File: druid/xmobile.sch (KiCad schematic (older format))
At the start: 12 parts, among them P3 CONN_8

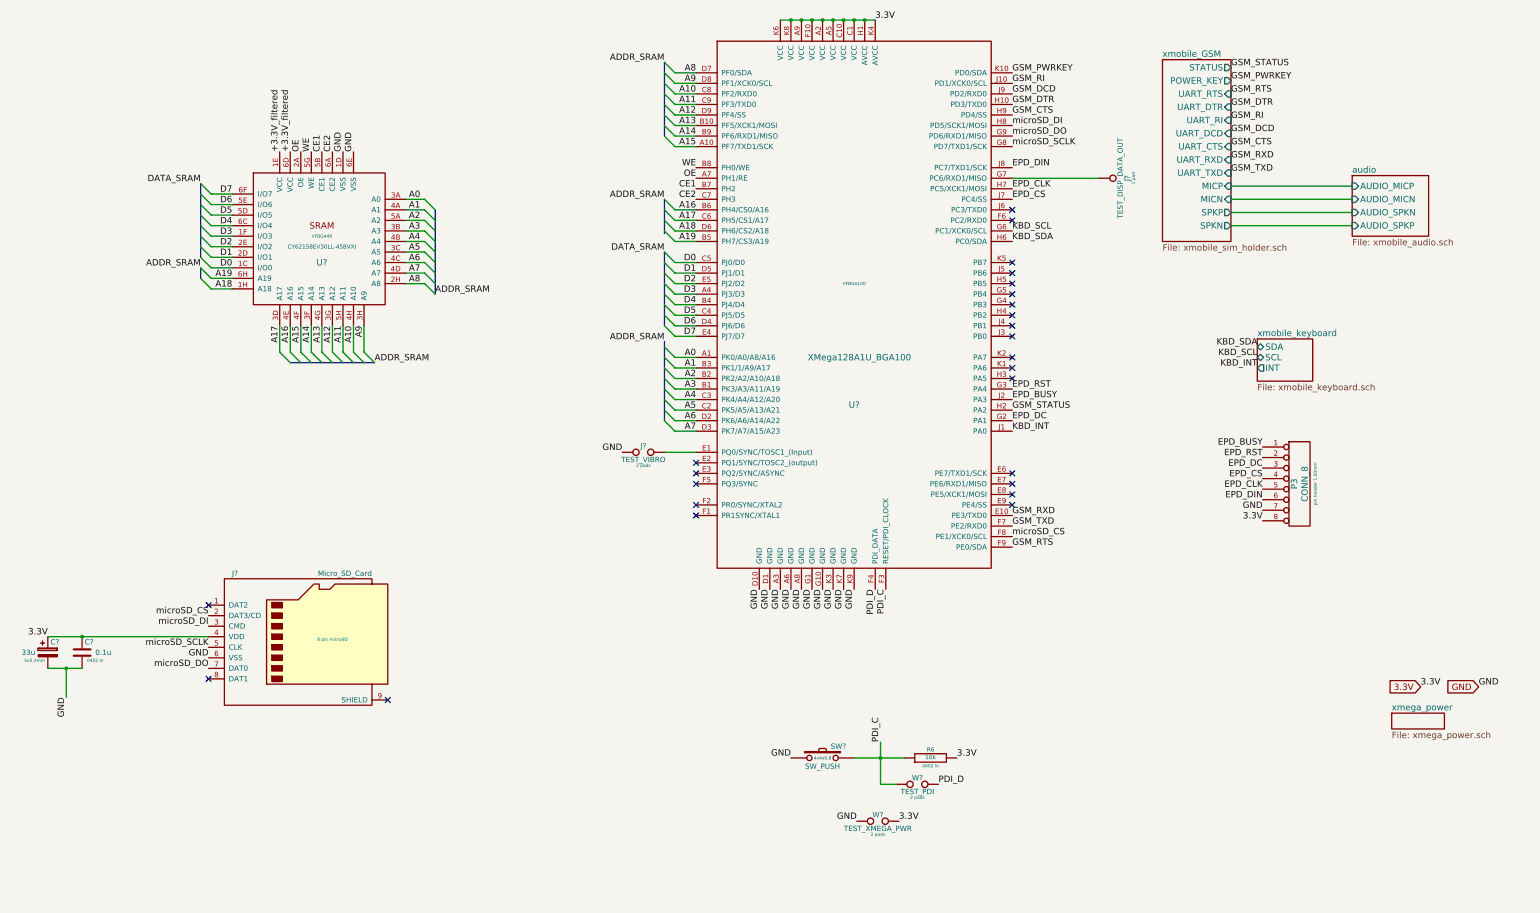
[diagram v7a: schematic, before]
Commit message: remove electric  warnings and errors. annotate elements. fix microUSB-B symbol.
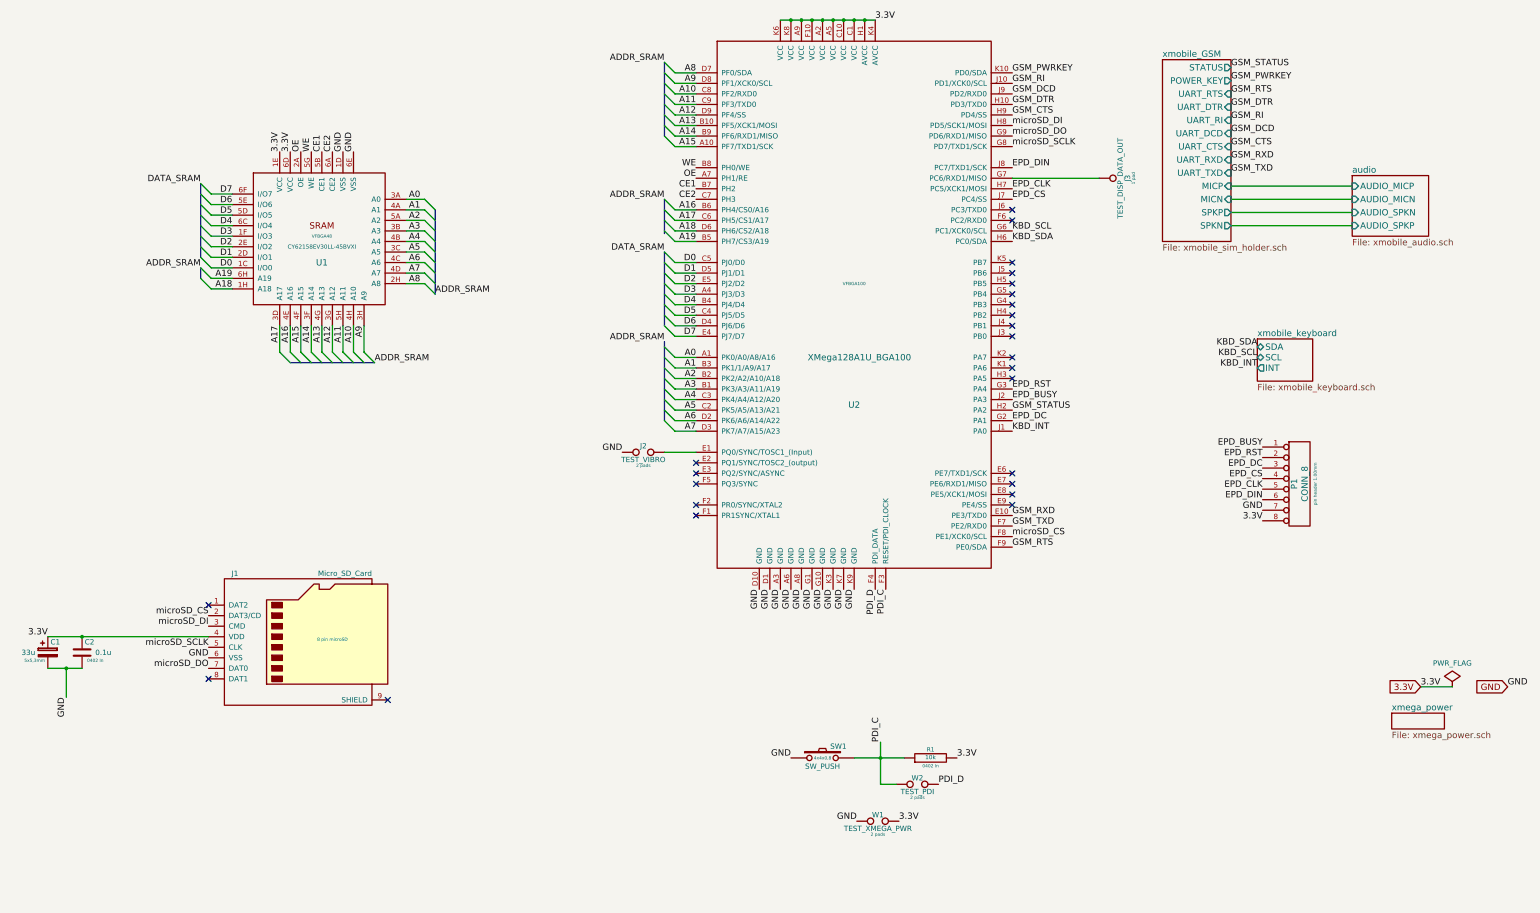
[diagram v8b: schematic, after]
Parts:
- gave numbers to parts that had none: 10
- renumbered P3 to P1, R6 to R1
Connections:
- net +3.3V_filtered is gone; now on net 3.3V: U1.1E (VCC), U1.6D (VCC)
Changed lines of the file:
@@
 $EndDescr
 $Comp
-L xmobile-rescue:R-RESCUE-xmobile R6
+L xmobile-rescue:R-RESCUE-xmobile R1
 U 1 1 5967CB22
 P 10025 10100
-F 0 "R6" V 10105 10100 40  0000 C CNN
+F 0 "R1" V 10105 10100 40  0000 C CNN
 F 1 "10k" V 10032 10101 40  0000 C CNN
 F 2 "Resistors_SMD:R_0402" V 9955 10100 30  0001 C CNN
@@
 3.3V
 $Comp
-L xmobile-rescue:CONN_8 P3
+L xmobile-rescue:CONN_8 P1
 U 1 1 5974D7B3
 P 13525 7500
-F 0 "P3" V 13475 7500 60  0000 C CNN
+F 0 "P1" V 13475 7500 60  0000 C CNN
 F 1 "CONN_8" V 13575 7500 60  0000 C CNN
 F 2 "Connector_Pin_Header_1.00mm:PinHeader_1x08_P1.00mm_Vertical" V 13700 7450 60  0001 C CNN
@@
 PDI_C
 $Comp
-L xmobile-rescue:CY62158EV30LL-45BVXI U?
+L xmobile-rescue:CY62158EV30LL-45BVXI U1
 U 1 1 5C118522
 P 4250 5200
-F 0 "U?" H 4250 5000 60  0000 C CNN
+F 0 "U1" H 4250 5000 60  0000 C CNN
 F 1 "CY62158EV30LL-45BVXI" H 4250 5150 39  0000 C CNN
 F 2 "druid:48-ball_VFBGA_6x8x1mm_BV48BZ48" H 4475 3925 60  0001 C CNN
@@
 $EndComp
 $Comp
-L xmobile-rescue:XMega128A1U_BGA100 U?
+L xmobile-rescue:XMega128A1U_BGA100 U2
 U 1 1 5C19D697
 P 9300 5600
-F 0 "U?" H 9300 4450 60  0000 C CNN
+F 0 "U2" H 9300 4450 60  0000 C CNN
 F 1 "XMega128A1U_BGA100" H 9350 4900 60  0000 C CNN
 F 2 "druid:BGA100_9x9x1.2_pitch-0.80mm" H 9400 5150 60  0001 C CNN
@@
 PDI_D
 Text Label 3850 4350 1    60   ~ 0
-+3.3V_filtered
+3.3V
 Text Label 3950 4350 1    60   ~ 0
-+3.3V_filtered
+3.3V
 Text Label 4550 4350 1    60   ~ 0
 GND
@@
 KBD_INT
 $Comp
-L xmobile-rescue:TEST_1P J?
+L xmobile-rescue:TEST_1P J3
 U 1 1 5C4B9CCC
 P 11625 4600
-F 0 "J?" H 11625 4870 50  0000 C CNN
+F 0 "J3" H 11625 4870 50  0000 C CNN
 F 1 "TEST_DISP_DATA_OUT" H 11625 4800 50  0000 C CNN
 F 2 "Measurement_Points:Measurement_Point_Square-TH_Small" H 11650 4925 50  0001 C CNN
@@
 Wire Wire Line
 	10800 4600 11625 4600
-Text GLabel 15225 9425 0    60   Input ~ 0
-GND
-Text Label 15225 9425 0    60   ~ 0
+Text GLabel 15500 9425 0    60   Input ~ 0
+GND
+Text Label 15500 9425 0    60   ~ 0
 GND
 Text Label 12875 3550 0    60   ~ 0
@@
 GSM_STATUS
 $Comp
-L xmobile-rescue:Micro_SD_Card J?
+L xmobile-rescue:Micro_SD_Card J1
 U 1 1 5C4DB2CD
 P 4075 8950
-F 0 "J?" H 3425 9550 50  0000 C CNN
+F 0 "J1" H 3425 9550 50  0000 C CNN
 F 1 "Micro_SD_Card" H 4725 9550 50  0000 R CNN
 F 2 "Connector_Card:microSD_HC_Wuerth_693072010801" H 4075 8200 50  0001 C CNN
@@
 GND
 $Comp
-L xmobile-rescue:C C?
+L xmobile-rescue:C C2
 U 1 1 5C4DFD85
 P 1975 9100
-F 0 "C?" H 2000 9200 50  0000 L CNN
+F 0 "C2" H 2000 9200 50  0000 L CNN
 F 1 "0.1u" H 2100 9100 50  0000 L CNN
 F 2 "Capacitors_SMD:C_0402" H 2175 9375 50  0001 C CNN
@@
 $EndComp
 $Comp
-L xmobile-rescue:CP C?
+L xmobile-rescue:CP C1
 U 1 1 5C4DFEA4
 P 1650 9100
-F 0 "C?" H 1675 9200 50  0000 L CNN
+F 0 "C1" H 1675 9200 50  0000 L CNN
 F 1 "33u" H 1400 9100 50  0000 L CNN
 F 2 "Capacitors_SMD:c_elec_5x5.3" H 1200 8875 50  0001 C CNN
@@
 microSD_CS
 $Comp
-L xmobile-rescue:SW_PUSH SW?
+L xmobile-rescue:SW_PUSH SW1
 U 1 1 5C505516
 P 9000 10100
-F 0 "SW?" H 9150 10210 50  0000 C CNN
+F 0 "SW1" H 9150 10210 50  0000 C CNN
 F 1 "SW_PUSH" H 9000 10020 50  0000 C CNN
 F 2 "druid:button_4pin_7,5x5" H 8975 9950 50  0001 C CNN
@@
 $EndComp
 $Comp
-L xmobile-rescue:TEST_2P J?
+L xmobile-rescue:TEST_2P J2
 U 1 1 5C561693
 P 7300 7200
-F 0 "J?" H 7300 7260 50  0000 C CNN
+F 0 "J2" H 7300 7260 50  0000 C CNN
 F 1 "TEST_VIBRO" H 7300 7130 50  0000 C CNN
 F 2 "Measurement_Points:Test_Point_2Pads" H 6925 7025 50  0001 C CNN
@@
 GND
 $Comp
-L xmobile-rescue:TEST-RESCUE-xmobile W?
+L xmobile-rescue:TEST-RESCUE-xmobile W2
 U 1 1 5C6C0FE4
 P 9900 10350
-F 0 "W?" H 9900 10410 50  0000 C CNN
+F 0 "W2" H 9900 10410 50  0000 C CNN
 F 1 "TEST_PDI" H 9900 10280 50  0000 C CNN
 F 2 "Measurement_Points:Test_Point_2Pads" H 10150 10200 50  0001 C CNN
@@
 $EndComp
 $Comp
-L xmobile-rescue:TEST-RESCUE-xmobile W?
+L xmobile-rescue:TEST-RESCUE-xmobile W1
 U 1 1 5C6C18FA
 P 9525 10700
-F 0 "W?" H 9525 10760 50  0000 C CNN
+F 0 "W1" H 9525 10760 50  0000 C CNN
 F 1 "TEST_XMEGA_PWR" H 9525 10630 50  0000 C CNN
 F 2 "Measurement_Points:Test_Point_2Pads" H 9625 10550 50  0001 C CNN
@@
 Wire Wire Line
 	1975 8950 3175 8950
+$Comp
+L xmobile-rescue:PWR_FLAG #FLG0101
+U 1 1 5C7368D2
+P 14975 9425
+F 0 "#FLG0101" H 14975 9520 50  0001 C CNN
+F 1 "PWR_FLAG" H 14975 9649 50  0000 C CNN
+F 2 "" H 14975 9425 50  0000 C CNN
+F 3 "" H 14975 9425 50  0000 C CNN
+	1    14975 9425
+	1    0    0    -1
+$EndComp
+Wire Wire Line
+	14675 9425 14975 9425
 Wire Bus Line
 	7500 4800 7500 5125
